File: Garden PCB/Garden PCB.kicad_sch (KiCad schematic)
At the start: 45 parts, among them IC1 LM74500QDDFRQ1, J1 GPIO, J10 Conn_02x05_Odd_Even, J11 Screw_Terminal_01x10, J12 Screw_Terminal_01x02, J2 Conn_02x06_Top_Bottom, J3 Conn_02x05_Odd_Even, J4 Conn_02x05_Odd_Even, J5 Conn_02x05_Odd_Even, J6 Conn_02x05_Odd_Even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

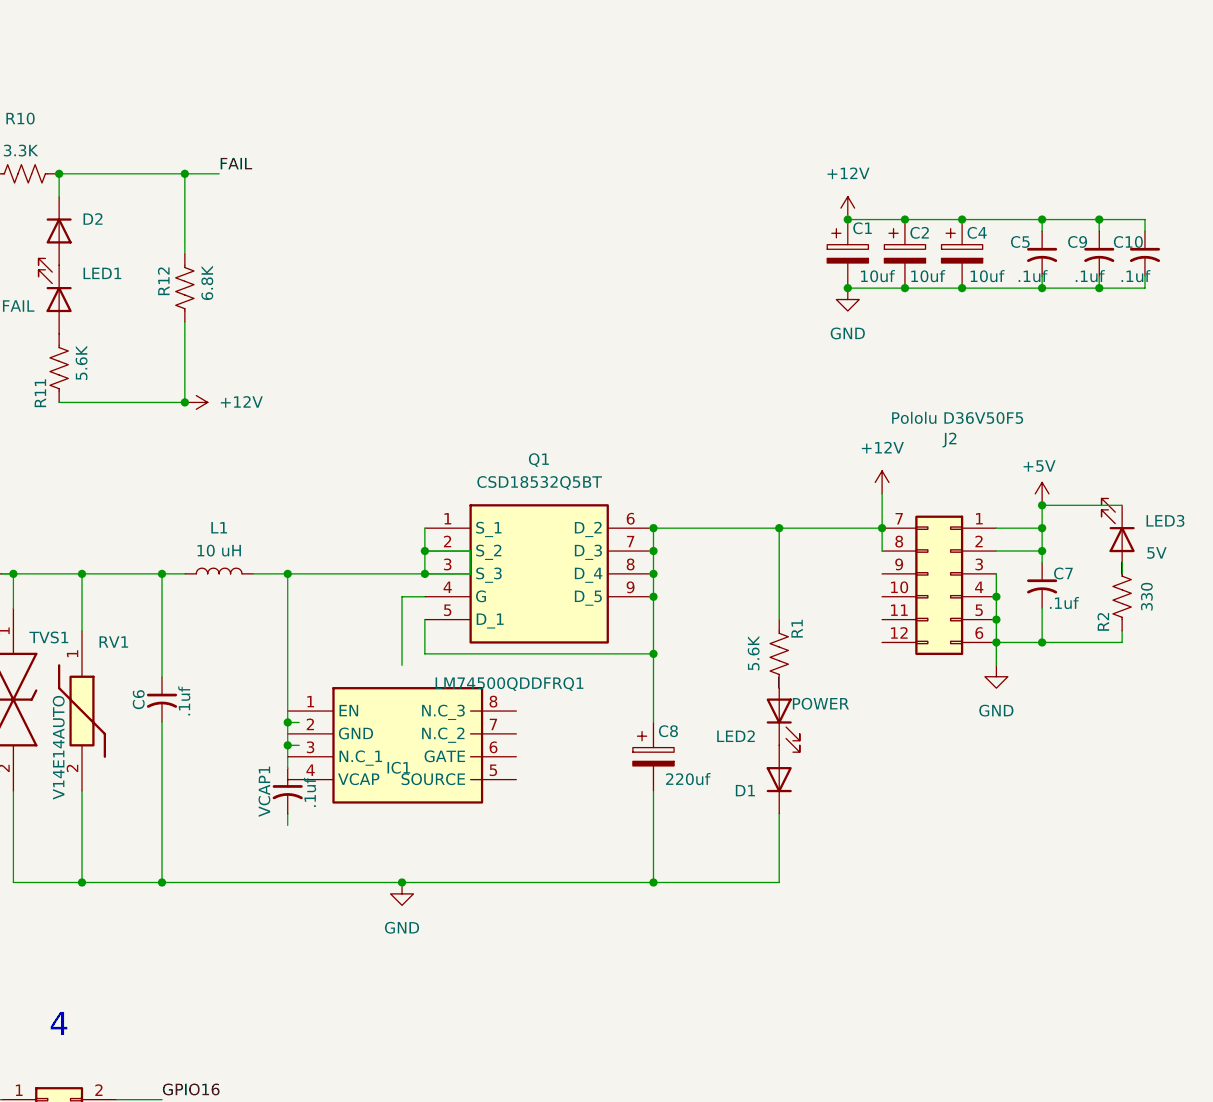
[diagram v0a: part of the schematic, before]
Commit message: fixes for power switch, also looks like KiCad might have boned some of our pinouts
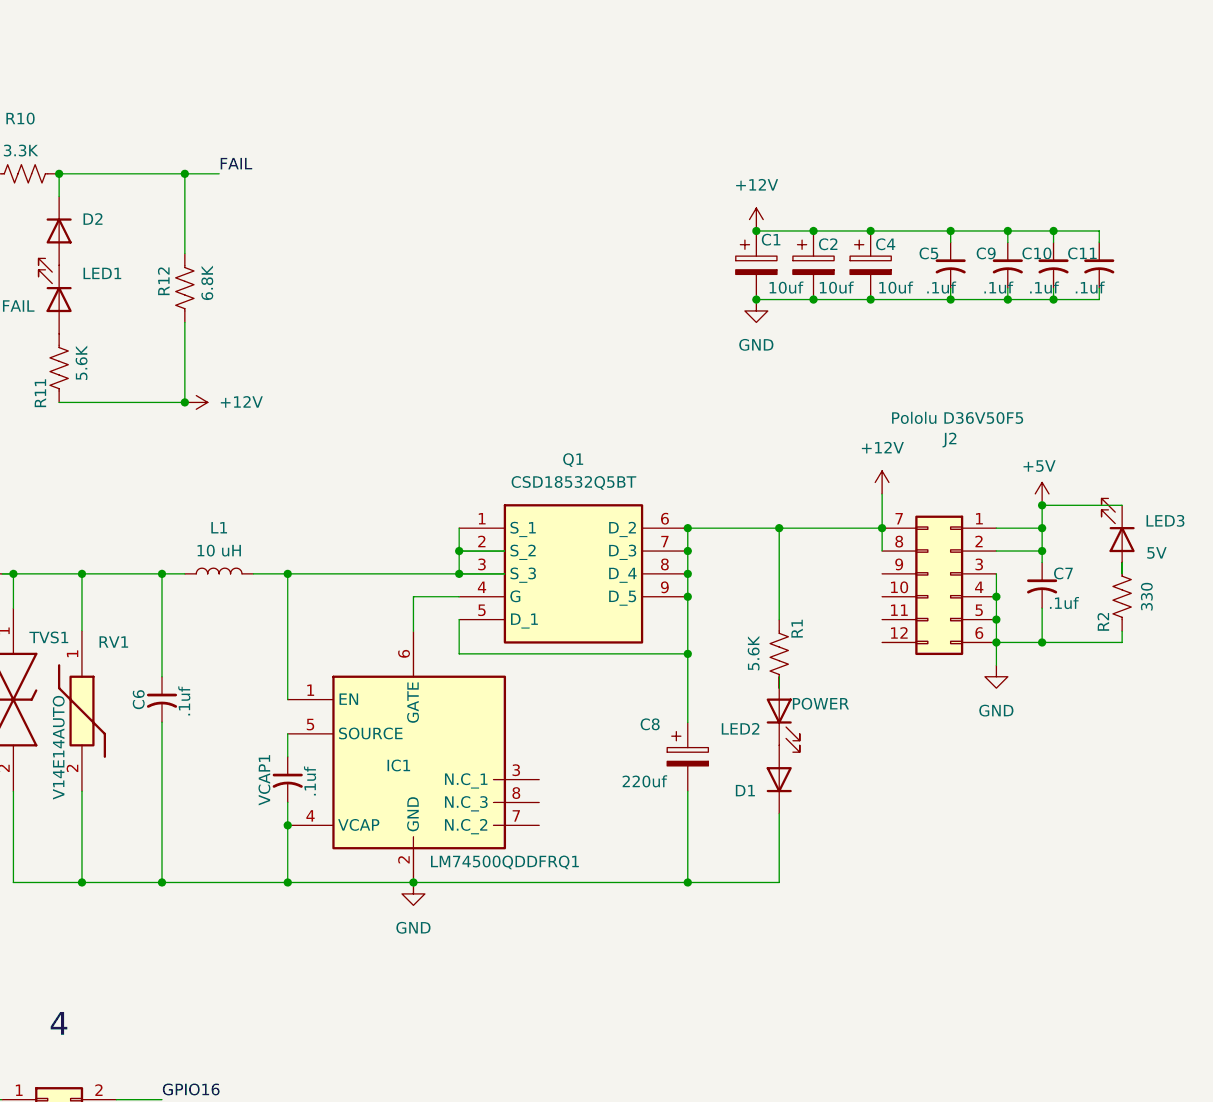
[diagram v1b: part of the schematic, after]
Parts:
- added C11: .1uf, RCER71H104K0DBH03A:RCER71H104K0DBH03A, symbol Device:C_Small_US
- D1, D2: footprint Diode_THT:D_DO-35_SOD27_P7.62mm_Horizontal -> Diode_SMD:D_SOD-323_HandSoldering
- SW1: footprint M2011SS1W01:M2011SS1W01CUL -> 7105SYV3QE:7105SYV3QE
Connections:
- net +12V: now also C11.1
- net GND: now also IC1.2 (GND), IC1.4 (VCAP), VCAP1.2, C11.2
- net at L1.2, Q1.1 (S_1), Q1.2 (S_2)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: now also IC1.1 (EN); no longer VCAP1.1
- net at Q1.4 (G): now also IC1.6 (GATE)
- net at IC1.5 (SOURCE): now also VCAP1.1
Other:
- moved on the sheet: C1, C10, C2, C4, C5, C8, C9, IC1, Q1, VCAP1
